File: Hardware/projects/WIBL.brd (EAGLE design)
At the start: 100.6 x 48.4 mm, 105 parts, among them IC1 SN65C1168N, T2 S8050, T3 S8050, T4 S8050, U1 ESP32-WROOM-32E, U2 TJA1051T/3, U3 LSM6DS3TR-C, U4 AMS1117-3.3

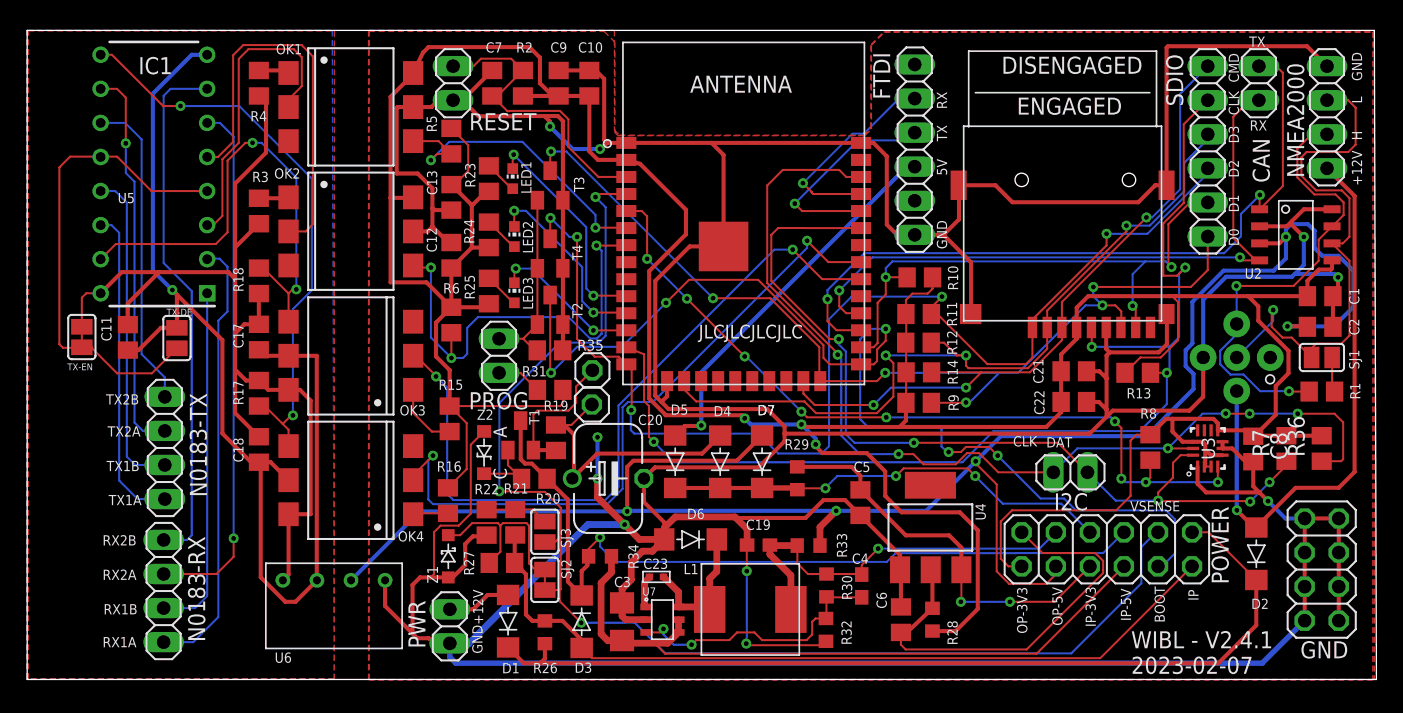
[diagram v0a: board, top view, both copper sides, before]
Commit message: Restore accidentally deleted files
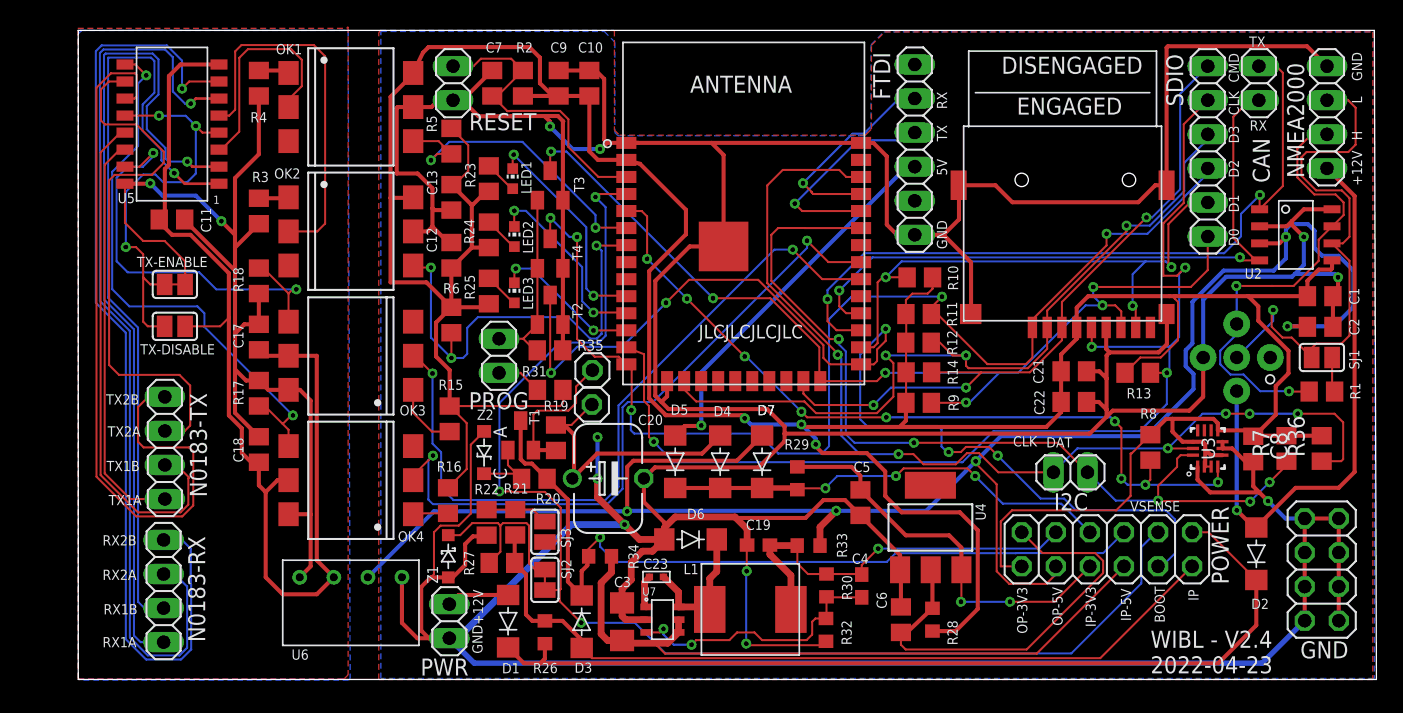
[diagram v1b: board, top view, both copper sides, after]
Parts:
- removed IC1: SN65C1168N, SN65C1168N:DIP794W53P254L1930H508Q16N
- removed TX-DE, TX-EN: (no value), jumper:SJ
- added TX-DISABLE, TX-ENABLE: (no value), jumper:SJ
- added U5: SN65C1168NSR, sb2030_logger:SOIC16
- moved C11 9.38 mm to (6.99, 34.3), turned to 180 degrees
- moved U6 1.28 mm to (20.3, 7.62)
- moved PWR 0.38 mm to (27.7, 4.34)
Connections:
- removed net N$12: IC1.6, N0183-RX.2
- removed net N$5: IC1.2, N0183-RX.4
- removed net N$8: IC1.14, N0183-TX.4
- removed net N$9: IC1.1, N0183-RX.3
- new net N$27: N0183-TX.4, U5.14
- new net N$28: N0183-TX.3, U5.13
- new net N$29: N0183-TX.2, U5.10
- new net N$30: N0183-TX.1, U5.11
- net GNDI: now also TX-DISABLE.1, U5.8; no longer IC1.8, TX-DE.1
- net N$13: now also U5.3; no longer IC1.3
- net N$14: now also U5.5; no longer IC1.5
- net N$17: now also N0183-RX.4, U5.2; no longer IC1.7, N0183-RX.1
- net N$18: now also N0183-RX.3, U5.1; no longer IC1.13, N0183-TX.3
- net N$19: now also N0183-RX.2, U5.6; no longer IC1.10, N0183-TX.2
- net N$20: now also N0183-RX.1, U5.7; no longer IC1.11, N0183-TX.1
- net N$21: now also TX-DISABLE.2, TX-ENABLE.1, TX-ENABLE.2, U5.12, U5.16, U5.4; no longer IC1.12, IC1.16, IC1.4, TX-DE.2, TX-EN.1, TX-EN.2
- net N$33: now also U5.15; no longer IC1.15
- net N$34: now also U5.9; no longer IC1.9
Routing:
- net N$30: track 0.00 -> 57.1 mm
- net N$20: track 23.5 -> 72.5 mm, vias 0 -> 1
- net N$29: track 0.00 -> 40.9 mm
- net N$12: track 39.5 -> 0.00 mm, vias 1 -> 0
- net N$19: track 29.2 -> 68.6 mm
- net N$28: track 0.00 -> 38.7 mm
- net N$18: track 24.3 -> 60.5 mm, vias 0 -> 1
- net N$5: track 33.0 -> 0.00 mm
- net N$27: track 0.00 -> 30.3 mm
- net N$9: track 26.2 -> 0.00 mm
- net N$17: track 39.3 -> 63.5 mm, vias 0 -> 1
- net N$8: track 24.1 -> 0.00 mm
- net N$13: track 23.0 -> 16.8 mm
- net N$33: track 36.5 -> 32.5 mm
- net GNDI: track 82.0 -> 79.5 mm, vias 1 -> 0
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- added copper zone on layer 16, net GND
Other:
- board size 100.6 x 48.4 mm -> 96.8 x 48.4 mm
- board text added: "(c) 2022 Center for Coastal and Ocean Mapping University of New Hampshire 2022-04-23 V2.4"
- board text added: "WIBL - V2.4 2022-04-23"
- board text removed: "(c) 2022 Center for Coastal and Ocean Mapping University of New Hampshire 2023-02-07 V2.4.1"
- board text removed: "WIBL - V2.4.1 2023-02-07"

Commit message: Added missing 2.4.1 hardware design files.
For reasons unknown, the v 2.4.1 schematic and board files never got checked into the repository; these are from a backup copy that reflects the initial state.
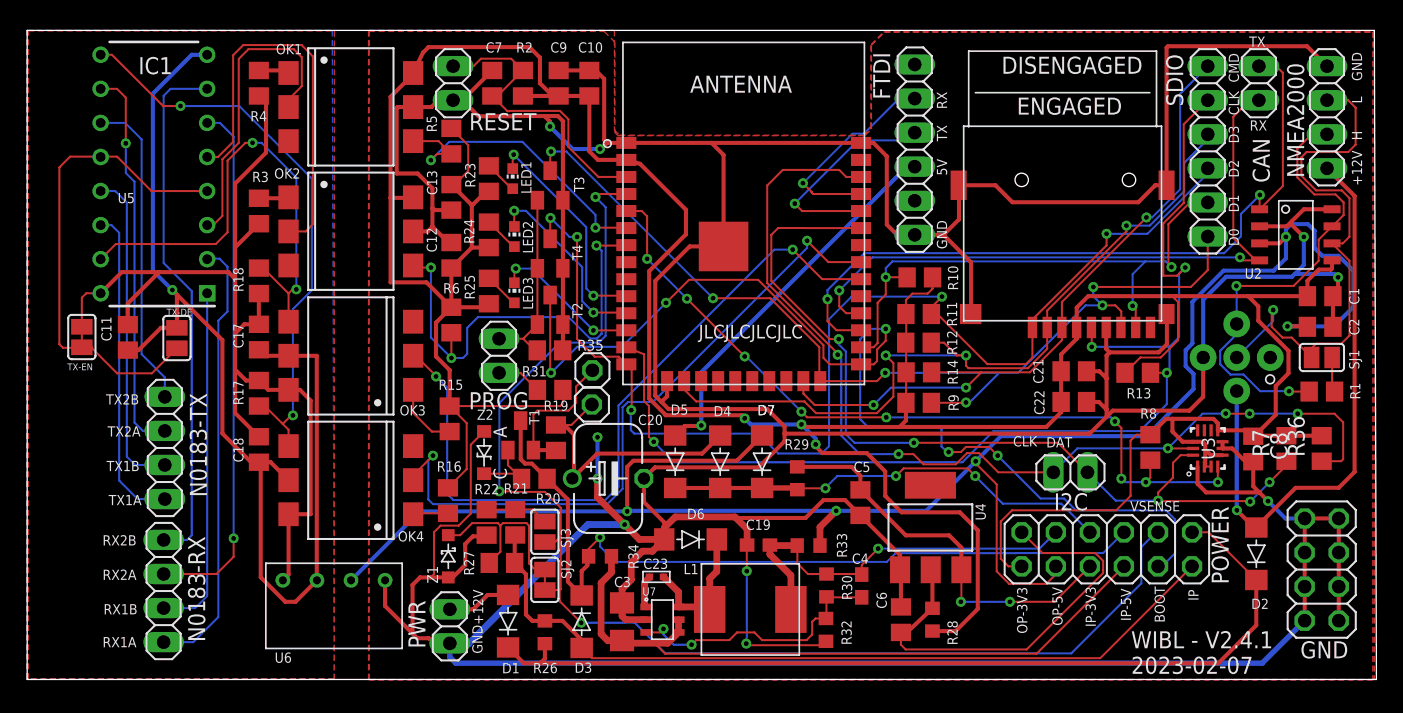
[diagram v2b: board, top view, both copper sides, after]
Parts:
- removed TX-DISABLE, TX-ENABLE: (no value), jumper:SJ
- removed U5: SN65C1168NSR, sb2030_logger:SOIC16
- added IC1: SN65C1168N, SN65C1168N:DIP794W53P254L1930H508Q16N
- added TX-DE, TX-EN: (no value), jumper:SJ
- moved C11 9.38 mm to (3.70, 25.5), turned to 270 degrees
- moved U6 1.28 mm to (19.1, 7.39)
- moved PWR 0.38 mm to (27.7, 3.96)
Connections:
- removed net N$27: N0183-TX.4, U5.14
- removed net N$28: N0183-TX.3, U5.13
- removed net N$29: N0183-TX.2, U5.10
- removed net N$30: N0183-TX.1, U5.11
- new net N$12: IC1.6, N0183-RX.2
- new net N$5: IC1.2, N0183-RX.4
- new net N$8: IC1.14, N0183-TX.4
- new net N$9: IC1.1, N0183-RX.3
- net GNDI: now also IC1.8, TX-DE.1; no longer TX-DISABLE.1, U5.8
- net N$13: now also IC1.3; no longer U5.3
- net N$14: now also IC1.5; no longer U5.5
- net N$17: now also IC1.7, N0183-RX.1; no longer N0183-RX.4, U5.2
- net N$18: now also IC1.13, N0183-TX.3; no longer N0183-RX.3, U5.1
- net N$19: now also IC1.10, N0183-TX.2; no longer N0183-RX.2, U5.6
- net N$20: now also IC1.11, N0183-TX.1; no longer N0183-RX.1, U5.7
- net N$21: now also IC1.12, IC1.16, IC1.4, TX-DE.2, TX-EN.1, TX-EN.2; no longer TX-DISABLE.2, TX-ENABLE.1, TX-ENABLE.2, U5.12, U5.16, U5.4
- net N$33: now also IC1.15; no longer U5.15
- net N$34: now also IC1.9; no longer U5.9
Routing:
- net N$30: track 57.1 -> 0.00 mm
- net N$20: track 72.5 -> 23.5 mm, vias 1 -> 0
- net N$29: track 40.9 -> 0.00 mm
- net N$12: track 0.00 -> 39.5 mm, vias 0 -> 1
- net N$19: track 68.6 -> 29.2 mm
- net N$28: track 38.7 -> 0.00 mm
- net N$18: track 60.5 -> 24.3 mm, vias 1 -> 0
- net N$5: track 0.00 -> 33.0 mm
- net N$27: track 30.3 -> 0.00 mm
- net N$9: track 0.00 -> 26.2 mm
- net N$17: track 63.5 -> 39.3 mm, vias 1 -> 0
- net N$8: track 0.00 -> 24.1 mm
- net N$13: track 16.8 -> 23.0 mm
- net N$33: track 32.5 -> 36.5 mm
- net GNDI: track 79.5 -> 82.0 mm, vias 0 -> 1
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- removed copper zone on layer 16, net GND
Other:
- board size 96.8 x 48.4 mm -> 100.6 x 48.4 mm
- board text added: "(c) 2022 Center for Coastal and Ocean Mapping University of New Hampshire 2023-02-07 V2.4.1"
- board text added: "WIBL - V2.4.1 2023-02-07"
- board text removed: "(c) 2022 Center for Coastal and Ocean Mapping University of New Hampshire 2022-04-23 V2.4"
- board text removed: "WIBL - V2.4 2022-04-23"
